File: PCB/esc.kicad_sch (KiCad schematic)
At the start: 31 parts, among them J1 Conn_01x04_Pin, J2 Conn_01x01, J3 Conn_01x01, J4 Conn_01x01, J5 Conn_01x01, J6 Conn_01x01, SW1 SW_SPST, U1 STM32C031K6T6, U2 TLV76133DCY, U3 TLV9064, U4 INA180A3

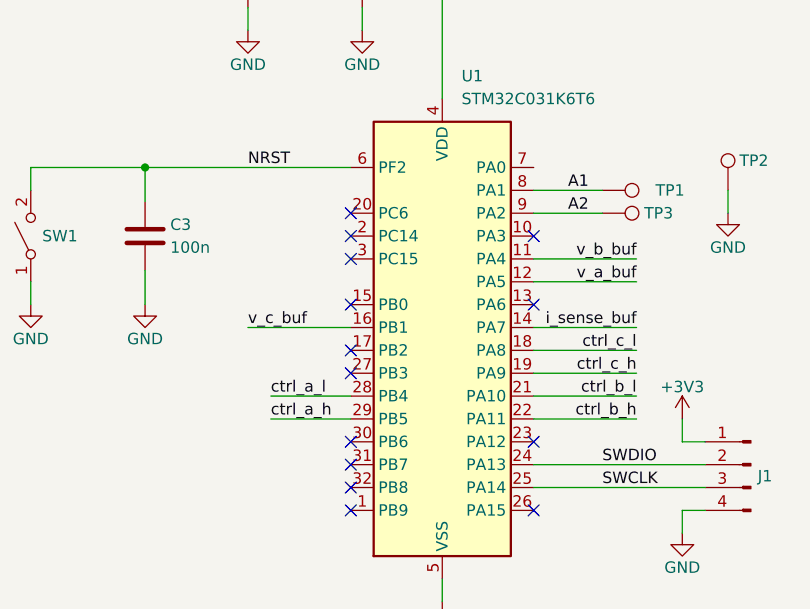
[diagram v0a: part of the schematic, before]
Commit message: Switched gate driving PWM to one timer
One timer is now used so the last OC channel can be used to trigger ADC
reads on the phase voltages. In theory, haven't implemented yet.
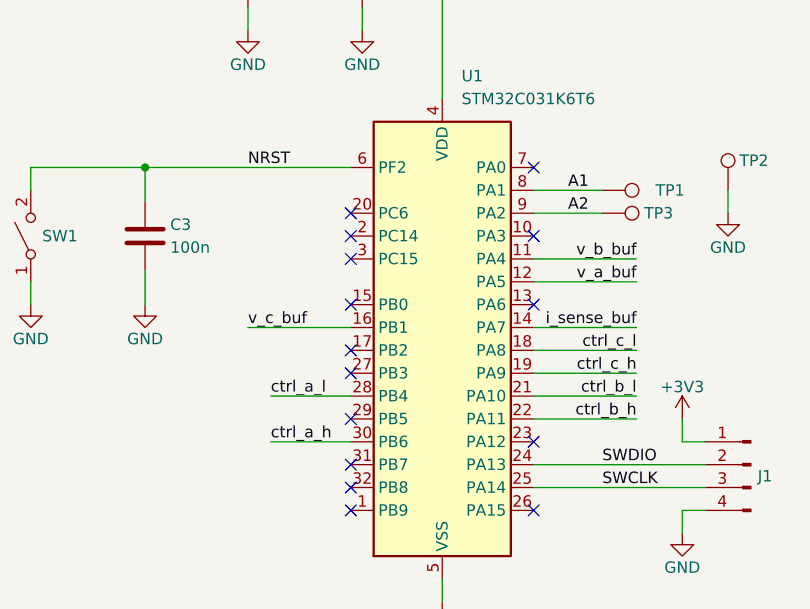
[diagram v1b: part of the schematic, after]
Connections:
- net ctrl_a_h: now also U1.30 (PB6); no longer U1.29 (PB5)
- no-connect marks 14 -> 15
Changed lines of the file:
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@@
 	)
 	(no_connect
-		(at 116.84 101.6)
+		(at 116.84 99.06)
 	)
 	(no_connect
@@
 	)
 	(no_connect
+		(at 137.16 71.12)
+	)
+	(no_connect
 		(at 116.84 76.2)
 	)
@@
 	(wire
 		(pts
+			(xy 107.95 101.6) (xy 116.84 101.6)
+		)
+		(stroke
+			(width 0)
+			(type default)
+		)
+	)
+	(wire
+		(pts
 			(xy 179.07 107.95) (xy 179.07 110.49)
 		)
@@
 		(pts
 			(xy 137.16 73.66) (xy 144.78 73.66)
-		)
-		(stroke
-			(width 0)
-			(type default)
-		)
-	)
-	(wire
-		(pts
-			(xy 107.95 99.06) (xy 116.84 99.06)
 		)
 		(stroke
@@
 		)
 	)
+	(label "ctrl_a_h"
+		(at 107.95 101.6 0)
+		(effects
+			(font
+				(size 1.27 1.27)
+			)
+			(justify left bottom)
+		)
+	)
 	(label "v_c"
 		(at 105.41 257.81 180)
@@
 		)
 	)
-	(label "ctrl_a_h"
-		(at 107.95 99.06 0)
-		(effects
-			(font
-				(size 1.27 1.27)
-			)
-			(justify left bottom)
-		)
-	)

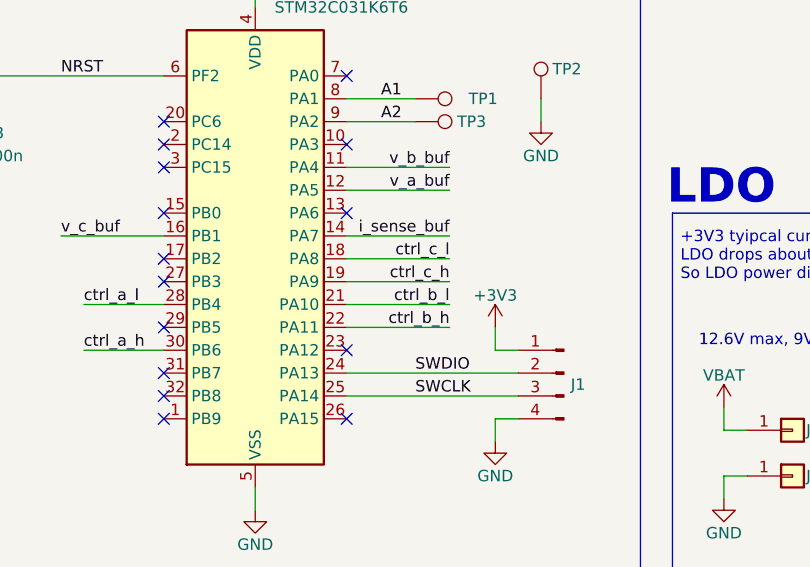
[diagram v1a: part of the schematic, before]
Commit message: Added template for zero crossing detection
Done some zero crossing detection in a sample_raw.c interrupt callback.
Interrupt fires to regularly so PWM frequency had to be reduced so other
stuff could run. Currently there's a bug where the sample buffer is
always reading {0, 0, 4095, 0}.
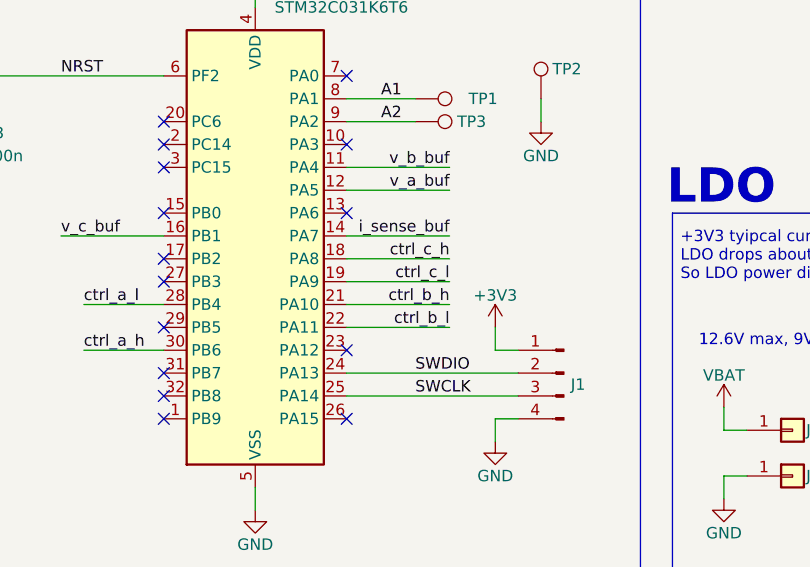
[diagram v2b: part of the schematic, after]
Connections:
- net ctrl_b_h: now also U1.21 (PA10); no longer U1.22 (PA11)
- net ctrl_b_l: now also U1.22 (PA11); no longer U1.21 (PA10)
- net ctrl_c_h: now also U1.18 (PA8); no longer U1.19 (PA9)
- net ctrl_c_l: now also U1.19 (PA9); no longer U1.18 (PA8)
